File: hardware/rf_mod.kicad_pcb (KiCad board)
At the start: 4 copper layers, 100 x 100 mm, 63 parts, among them J1201 SMA, J1202 SMA, J201 SMA, J202 SMA, J401 SMA, J402 SMA, J501 SMA, J502 SMA, J901 USB-C, J902 SMA, Q1201 AO3401A, Q501 AO3401A, SW1201 ON, SW501 ON, U1201 GALI-84+, U501 GALI-84+, U901 MT3608, U902 3.3V, U903 74LVC1G17, X901 25 MHz

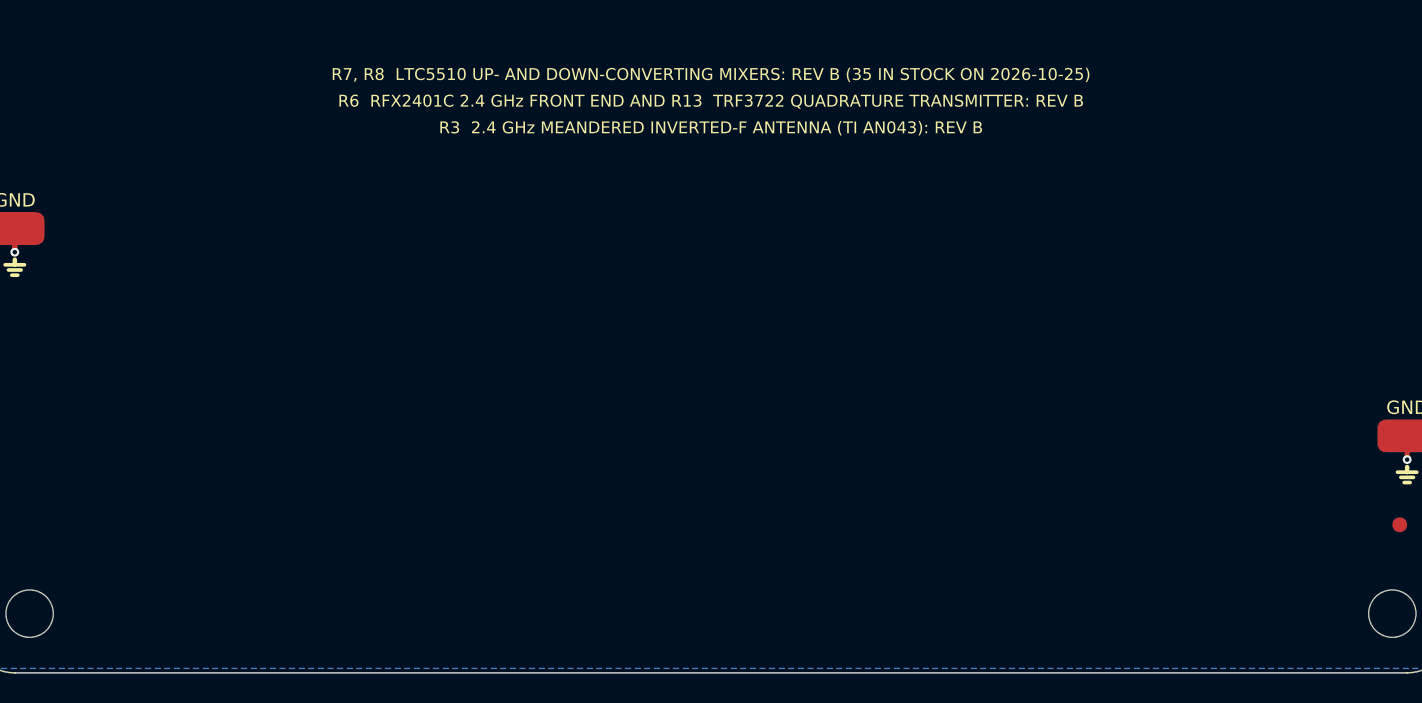
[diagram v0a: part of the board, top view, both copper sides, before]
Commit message: RF-MOD: the two MAX2871 synthesizer tiles (R10 host of the Pmod plug, R11) at DRC 0; a Fine net class at 0.127 mm with 0.45/0.25 vias for the QFN fan-out, V33 islands on L3, FRONT_WIRES; the fab package passes
Co-Authored-By: Claude Fable 5.1 <noreply@anthropic.com>
Claude-Session: https://claude.ai/code/session_01RKeoKvFFzjk3cEBLCXXHnB
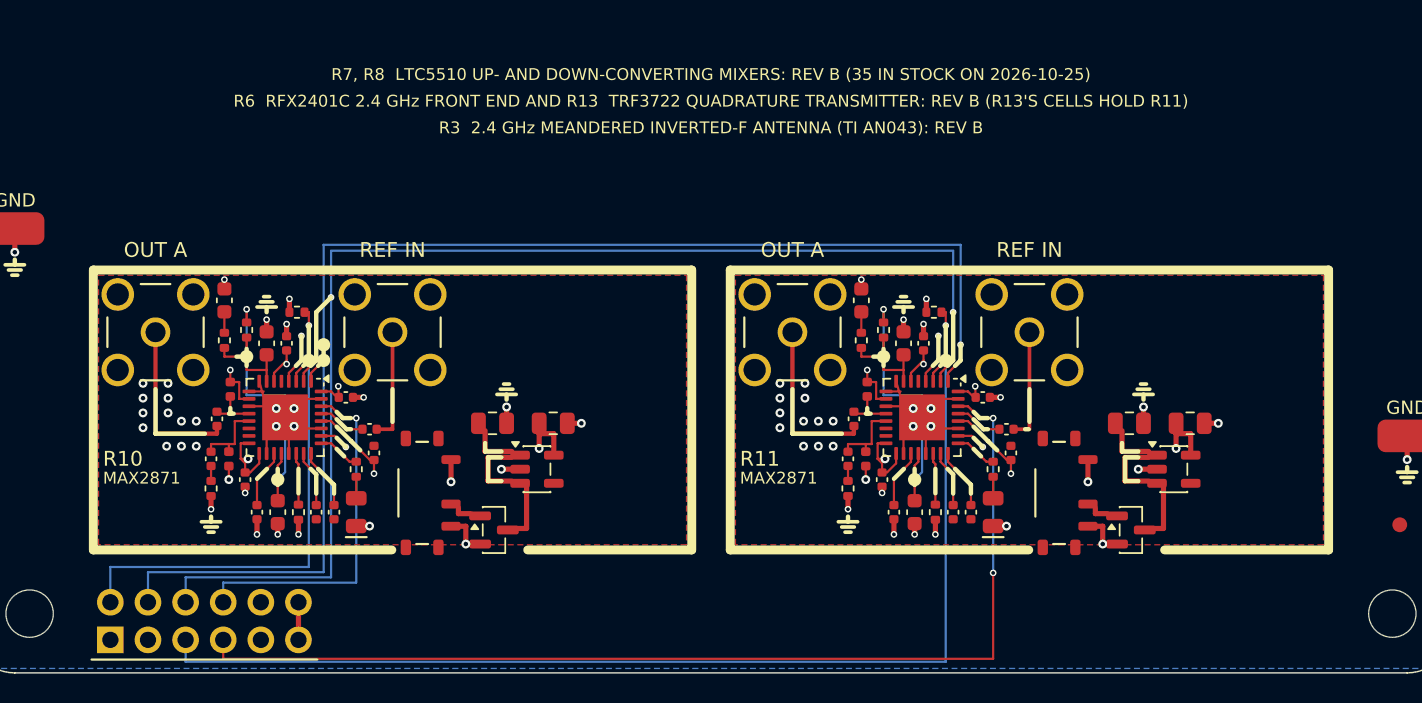
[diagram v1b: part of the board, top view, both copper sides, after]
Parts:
- added C1001: 1u, Capacitor_SMD:C_0805_2012Metric, F.Cu at (35.2, 83.2)
- added C1002: 1u, Capacitor_SMD:C_0805_2012Metric, F.Cu at (39.4, 83.2)
- added C1003: 470p, Capacitor_SMD:C_0603_1608Metric, F.Cu at (20.0, 77.8)
- added C1004: 6.8n, Capacitor_SMD:C_0603_1608Metric, F.Cu at (17.1, 74.8)
- added C1005: 100n, Capacitor_SMD:C_0402_1005Metric, F.Cu at (21.4, 77.8)
- added C1006: 100n, Capacitor_SMD:C_0402_1005Metric, F.Cu at (25.4, 81.4)
- added C1007: 100n, Capacitor_SMD:C_0402_1005Metric, F.Cu at (26.9, 83.5)
- added C1008: 100n, Capacitor_SMD:C_0402_1005Metric, F.Cu at (27.2, 85.2)
- added C1009: 100p, Capacitor_SMD:C_0402_1005Metric, F.Cu at (16.6, 82.8)
- added C1010: 100p, Capacitor_SMD:C_0402_1005Metric, F.Cu at (16.2, 85.5)
- added C1011: 100n, Capacitor_SMD:C_0402_1005Metric, F.Cu at (18.6, 87.0)
- added C1012: 1u, Capacitor_SMD:C_0402_1005Metric, F.Cu at (19.4, 89.2)
- added C1013: 100p, Capacitor_SMD:C_0603_1608Metric, F.Cu at (20.8, 89.2)
- added C1014: 1u, Capacitor_SMD:C_0402_1005Metric, F.Cu at (23.4, 89.2)
- added C1015: 1u, Capacitor_SMD:C_0402_1005Metric, F.Cu at (24.6, 89.2)
- added C1101: 1u, Capacitor_SMD:C_0805_2012Metric, F.Cu at (78.2, 83.2)
- added C1102: 1u, Capacitor_SMD:C_0805_2012Metric, F.Cu at (82.3, 83.2)
- added C1103: 470p, Capacitor_SMD:C_0603_1608Metric, F.Cu at (63.0, 77.8)
- added C1104: 6.8n, Capacitor_SMD:C_0603_1608Metric, F.Cu at (60.1, 74.8)
- added C1105: 100n, Capacitor_SMD:C_0402_1005Metric, F.Cu at (64.3, 77.8)
- added C1106: 100n, Capacitor_SMD:C_0402_1005Metric, F.Cu at (68.3, 81.4)
- added C1107: 100n, Capacitor_SMD:C_0402_1005Metric, F.Cu at (70.0, 83.5)
- added C1108: 100n, Capacitor_SMD:C_0402_1005Metric, F.Cu at (70.2, 85.2)
- added C1109: 100p, Capacitor_SMD:C_0402_1005Metric, F.Cu at (59.6, 82.8)
- added C1110: 100p, Capacitor_SMD:C_0402_1005Metric, F.Cu at (59.2, 85.5)
- added C1111: 100n, Capacitor_SMD:C_0402_1005Metric, F.Cu at (61.5, 87.0)
- added C1112: 1u, Capacitor_SMD:C_0402_1005Metric, F.Cu at (62.4, 89.2)
- added C1113: 100p, Capacitor_SMD:C_0603_1608Metric, F.Cu at (63.8, 89.2)
- added C1114: 1u, Capacitor_SMD:C_0402_1005Metric, F.Cu at (66.3, 89.2)
- added C1115: 1u, Capacitor_SMD:C_0402_1005Metric, F.Cu at (67.5, 89.2)
- added J1001: SMA, amod:SMA_BWSMA-KE-Z001_Vertical, F.Cu at (12.5, 77.0)
- added J1002: SMA, amod:SMA_BWSMA-KE-Z001_Vertical, F.Cu at (28.5, 77.0)
- added J1003: Pmod, amod:PinHeader_2x06_P2.54mm_Horizontal_PZ254R-12-12P, F.Cu at (15.8, 96.5)
- added J1101: SMA, amod:SMA_BWSMA-KE-Z001_Vertical, F.Cu at (55.5, 77.0)
- added J1102: SMA, amod:SMA_BWSMA-KE-Z001_Vertical, F.Cu at (71.5, 77.0)
- added L1001: 27n, Inductor_SMD:L_0402_1005Metric, F.Cu at (17.6, 80.8)
- added L1002: 27n, Inductor_SMD:L_0402_1005Metric, F.Cu at (17.4, 85.5)
- added L1101: 27n, Inductor_SMD:L_0402_1005Metric, F.Cu at (60.5, 80.8)
- added L1102: 27n, Inductor_SMD:L_0402_1005Metric, F.Cu at (60.5, 85.5)
- added LED1001: LOCK, amod:LED_0805_2012Metric_Kbar, F.Cu at (26.1, 89.2)
- added LED1101: LOCK, amod:LED_0805_2012Metric_Kbar, F.Cu at (69.0, 89.2)
- added Q1001: AO3401A, Package_TO_SOT_SMD:SOT-23, F.Cu at (35.4, 90.3)
- added Q1101: AO3401A, Package_TO_SOT_SMD:SOT-23, F.Cu at (78.3, 90.3)
- added R1001: 470, Resistor_SMD:R_0402_1005Metric, F.Cu at (18.6, 76.8)
- added R1002: 820, Resistor_SMD:R_0402_1005Metric, F.Cu at (17.1, 77.5)
- added R1003: 100k, Resistor_SMD:R_0402_1005Metric, F.Cu at (22.1, 75.7)
- added R1004: 1k, Resistor_SMD:R_0402_1005Metric, F.Cu at (26.1, 86.2)
- added R1005: 51R, Resistor_SMD:R_0402_1005Metric, F.Cu at (16.2, 87.5)
- added R1006: 5.1k, Resistor_SMD:R_0402_1005Metric, F.Cu at (22.1, 89.2)
- added R1101: 470, Resistor_SMD:R_0402_1005Metric, F.Cu at (61.6, 76.8)
- added R1102: 820, Resistor_SMD:R_0402_1005Metric, F.Cu at (60.1, 77.5)
- added R1103: 100k, Resistor_SMD:R_0402_1005Metric, F.Cu at (65.0, 75.7)
- added R1104: 1k, Resistor_SMD:R_0402_1005Metric, F.Cu at (69.0, 86.2)
- added R1105: 51R, Resistor_SMD:R_0402_1005Metric, F.Cu at (59.2, 87.5)
- added R1106: 5.1k, Resistor_SMD:R_0402_1005Metric, F.Cu at (65.2, 89.2)
- added SW1001: ON, amod:SW_SPDT_Shouhan_MSK12C02, F.Cu at (30.5, 87.8)
- added SW1101: ON, amod:SW_SPDT_Shouhan_MSK12C02, F.Cu at (73.5, 87.8)
- added U1001: 3.3V, Package_TO_SOT_SMD:SOT-23-5, F.Cu at (38.2, 86.2)
- added U1002: MAX2871, Package_DFN_QFN:QFN-32-1EP_5x5mm_P0.5mm_EP3.1x3.1mm, F.Cu at (21.2, 82.8)
- added U1101: 3.3V, Package_TO_SOT_SMD:SOT-23-5, F.Cu at (81.2, 86.2)
- added U1102: MAX2871, Package_DFN_QFN:QFN-32-1EP_5x5mm_P0.5mm_EP3.1x3.1mm, F.Cu at (64.2, 82.8)
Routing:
- net /PMOD6: track 0.00 -> 91.4 mm, vias 0 -> 2
- net /PMOD7: track 0.00 -> 91.1 mm, vias 0 -> 2
- net /PMOD3: track 0.00 -> 80.8 mm, vias 0 -> 1
- net /PMOD4: track 0.00 -> 72.2 mm, vias 0 -> 2
- net GND: track 55.4 -> 105.4 mm, vias 92 -> 154
- net /PMOD5: track 0.00 -> 37.4 mm, vias 0 -> 1
- net /R10_V33: track 0.00 -> 29.5 mm, vias 0 -> 9
- net /R11_V33: track 0.00 -> 29.5 mm, vias 0 -> 9
- net /PMOD8: track 0.00 -> 24.1 mm, vias 0 -> 1
- net /R11_TN: track 0.00 -> 18.5 mm, vias 0 -> 2
- net /R10_TN: track 0.00 -> 18.5 mm, vias 0 -> 2
- net /R11_OUTA: track 0.00 -> 11.5 mm
- net /R10_OUTA: track 0.00 -> 11.5 mm
- net /R11_VS: track 0.00 -> 11.4 mm
- net /R10_VS: track 0.00 -> 11.4 mm
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- added copper zone on In2.Cu, net /R10_V33
- added copper zone on In2.Cu, net /R11_V33
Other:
- board text added: "MAX2871"
- board text added: "OUT A"
- board text added: "R10"
- board text added: "R11"
- board text added: "R6 RFX2401C 2.4 GHz FRONT END AND R13 TRF3722 QUADRATURE TRANSMITTER: REV B (R13'S CELLS HOLD R11)"
- board text added: "REF IN"
- board text removed: "R6 RFX2401C 2.4 GHz FRONT END AND R13 TRF3722 QUADRATURE TRANSMITTER: REV B"

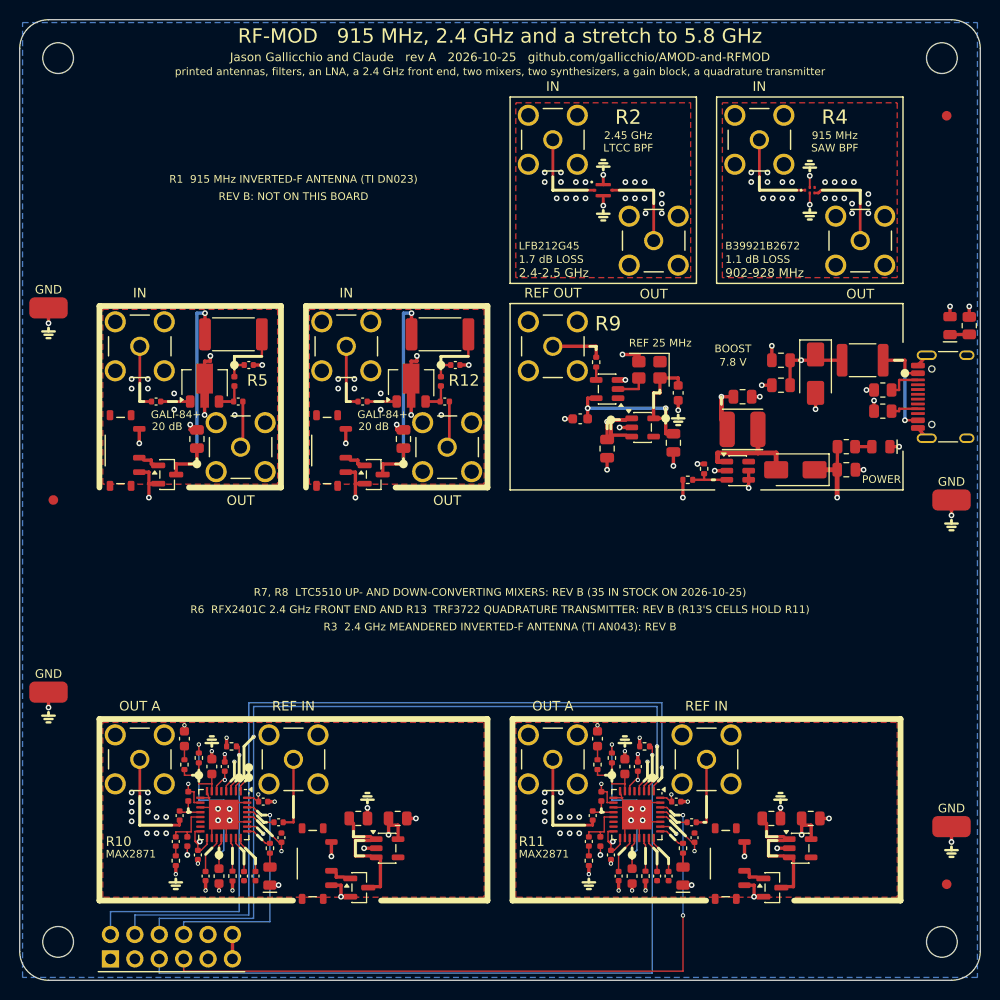
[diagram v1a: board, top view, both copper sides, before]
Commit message: RF-MOD filled: ADL5350 mixers R7/R8, a resistive splitter R1, ten tiles on sixteen cells at ERC/DRC 0 and the fab package passing; stand-in 3D bodies scaled 1/2.54 (VRML unit) on every board
Co-Authored-By: Claude Opus 5.5 <noreply@anthropic.com>
Claude-Session: https://claude.ai/code/session_01RKeoKvFFzjk3cEBLCXXHnB
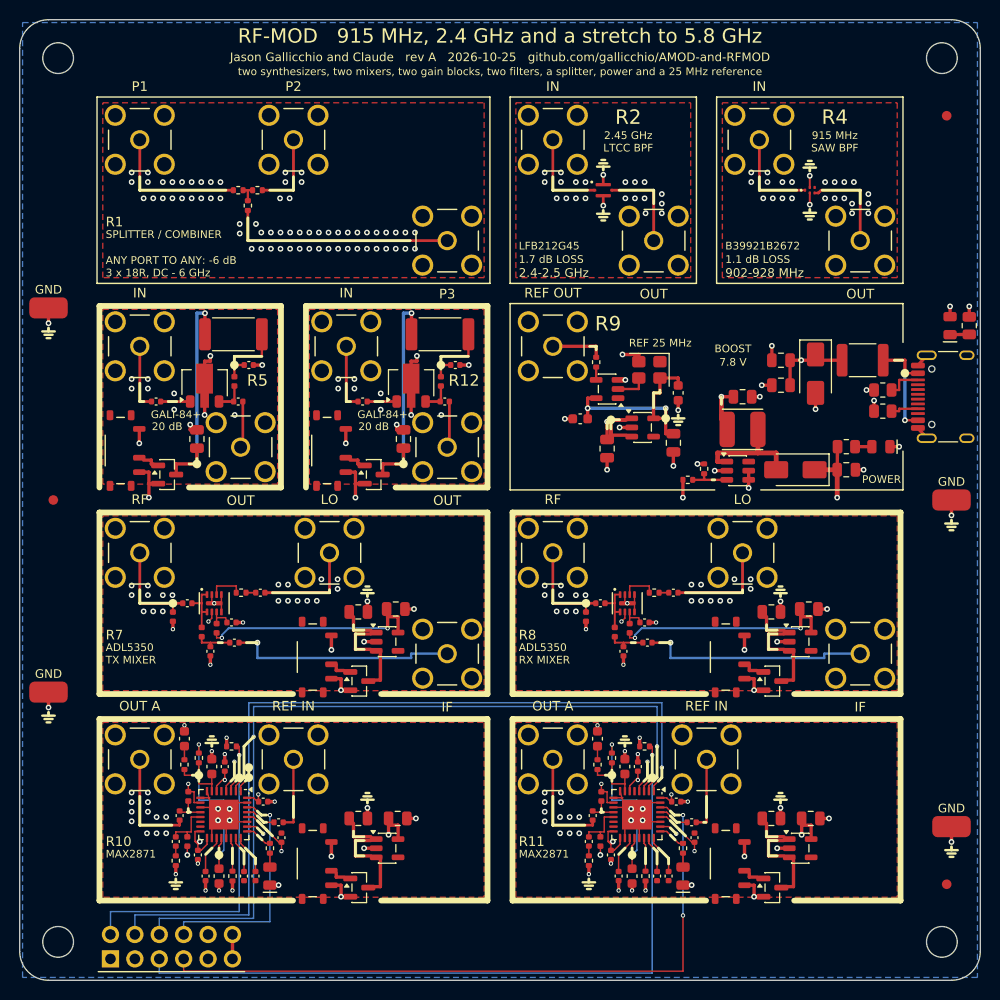
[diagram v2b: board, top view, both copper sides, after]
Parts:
- added C701: 1u, Capacitor_SMD:C_0805_2012Metric, F.Cu at (35.2, 61.6)
- added C702: 4.7u, Capacitor_SMD:C_0805_2012Metric, F.Cu at (39.1, 61.4)
- added C703: 15p, Capacitor_SMD:C_0402_1005Metric, F.Cu at (17.4, 60.8)
- added C704: 15p, Capacitor_SMD:C_0402_1005Metric, F.Cu at (19.9, 65.8)
- added C705: 100n, Capacitor_SMD:C_0402_1005Metric, F.Cu at (22.4, 64.8)
- added C706: 100p, Capacitor_SMD:C_0402_1005Metric, F.Cu at (25.1, 59.6)
- added C707: 100p, Capacitor_SMD:C_0402_1005Metric, F.Cu at (22.1, 62.8)
- added C801: 1u, Capacitor_SMD:C_0805_2012Metric, F.Cu at (78.2, 61.6)
- added C802: 4.7u, Capacitor_SMD:C_0805_2012Metric, F.Cu at (82.2, 61.4)
- added C803: 15p, Capacitor_SMD:C_0402_1005Metric, F.Cu at (60.5, 60.8)
- added C804: 15p, Capacitor_SMD:C_0402_1005Metric, F.Cu at (62.9, 65.8)
- added C805: 100n, Capacitor_SMD:C_0402_1005Metric, F.Cu at (65.3, 64.8)
- added C806: 100p, Capacitor_SMD:C_0402_1005Metric, F.Cu at (68.0, 59.6)
- added C807: 100p, Capacitor_SMD:C_0402_1005Metric, F.Cu at (65.0, 62.8)
- added J101: SMA, amod:SMA_BWSMA-KE-Z001_Vertical, F.Cu at (12.5, 12.5)
- added J102: SMA, amod:SMA_BWSMA-KE-Z001_Vertical, F.Cu at (28.5, 12.5)
- added J103: SMA, amod:SMA_BWSMA-KE-Z001_Vertical, F.Cu at (44.5, 23.0)
- added J701: SMA, amod:SMA_BWSMA-KE-Z001_Vertical, F.Cu at (12.5, 55.5)
- added J702: SMA, amod:SMA_BWSMA-KE-Z001_Vertical, F.Cu at (32.2, 55.5)
- added J703: SMA, amod:SMA_BWSMA-KE-Z001_Vertical, F.Cu at (44.5, 66.0)
- added J801: SMA, amod:SMA_BWSMA-KE-Z001_Vertical, F.Cu at (55.5, 55.5)
- added J802: SMA, amod:SMA_BWSMA-KE-Z001_Vertical, F.Cu at (75.2, 55.5)
- added J803: SMA, amod:SMA_BWSMA-KE-Z001_Vertical, F.Cu at (87.5, 66.0)
- added L701: 47n, Inductor_SMD:L_0402_1005Metric, F.Cu at (15.9, 62.1)
- added L702: 47n, Inductor_SMD:L_0402_1005Metric, F.Cu at (18.9, 63.8)
- added L703: 10n, Inductor_SMD:L_0402_1005Metric, F.Cu at (20.5, 63.4)
- added L801: 47n, Inductor_SMD:L_0402_1005Metric, F.Cu at (59.0, 62.1)
- added L802: 47n, Inductor_SMD:L_0402_1005Metric, F.Cu at (62.0, 63.8)
- added L803: 10n, Inductor_SMD:L_0402_1005Metric, F.Cu at (63.5, 63.4)
- added Q701: AO3401A, Package_TO_SOT_SMD:SOT-23, F.Cu at (35.4, 68.8)
- added Q801: AO3401A, Package_TO_SOT_SMD:SOT-23, F.Cu at (78.3, 68.8)
- added R101: 18R, Resistor_SMD:R_0402_1005Metric, F.Cu at (22.8, 17.8)
- added R102: 18R, Resistor_SMD:R_0402_1005Metric, F.Cu at (24.8, 17.8)
- added R103: 18R, Resistor_SMD:R_0402_1005Metric, F.Cu at (23.8, 19.4)
- added R701: 0R, Resistor_SMD:R_0402_1005Metric, F.Cu at (23.1, 59.6)
- added R801: 0R, Resistor_SMD:R_0402_1005Metric, F.Cu at (66.0, 59.6)
- added SW701: ON, amod:SW_SPDT_Shouhan_MSK12C02, F.Cu at (30.5, 66.3)
- added SW801: ON, amod:SW_SPDT_Shouhan_MSK12C02, F.Cu at (73.5, 66.3)
- added U701: 3.3V, Package_TO_SOT_SMD:SOT-23-5, F.Cu at (38.2, 64.8)
- added U702: ADL5350, amod:LFCSP-8_2x3mm_P0.5mm_ADL5350, F.Cu at (20.2, 60.8)
- added U801: 3.3V, Package_TO_SOT_SMD:SOT-23-5, F.Cu at (81.2, 64.8)
- added U802: ADL5350, amod:LFCSP-8_2x3mm_P0.5mm_ADL5350, F.Cu at (63.2, 60.8)
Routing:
- net /R1_P3: track 0.00 -> 23.9 mm
- net /R8_IF: track 0.00 -> 23.7 mm, vias 0 -> 1
- net /R7_IF: track 0.00 -> 23.7 mm, vias 0 -> 1
- net /R7_V33: track 0.00 -> 23.6 mm, vias 0 -> 2
- net /R8_V33: track 0.00 -> 23.6 mm, vias 0 -> 2
- net GND: track 105.4 -> 127.6 mm, vias 154 -> 274
- net /R1_P1: track 0.00 -> 15.0 mm
- net /R8_VS: track 0.00 -> 11.4 mm
- net /R7_VS: track 0.00 -> 11.4 mm
- net /R8_LOJ: track 0.00 -> 10.9 mm
- net /R7_LOJ: track 0.00 -> 10.9 mm
- net /R8_RFN: track 0.00 -> 10.6 mm
- net /R7_RFN: track 0.00 -> 10.6 mm
- net /R1_P2: track 0.00 -> 8.49 mm
- net +5V: track 31.9 -> 38.2 mm, vias 7 -> 9
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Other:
- board text added: "3 x 18R, DC - 6 GHz"
- board text added: "ADL5350"
- board text added: "ANY PORT TO ANY: -6 dB"
- board text added: "IF"
- board text added: "LO"
- board text added: "P1"
- board text added: "P2"
- board text added: "P3"
- board text added: "R1"
- board text added: "R7"
- board text added: "R8"
- board text added: "RF"
- board text added: "RX MIXER"
- board text added: "SPLITTER / COMBINER"
- board text added: "TX MIXER"
- board text added: "jack, OUT its bottom-right; the powered tiles have a slide"
- board text added: "switch (up: on). Power: USB-C on R9. The handbook has"
- board text added: "the rest."
- board text added: "two synthesizers, two mixers, two gain blocks, two filters, a splitter, power and a 25 MHz reference"
- board text removed: "R1 915 MHz INVERTED-F ANTENNA (TI DN023)"
- board text removed: "R3 2.4 GHz MEANDERED INVERTED-F ANTENNA (TI AN043): REV B"
- board text removed: "R6 RFX2401C 2.4 GHz FRONT END AND R13 TRF3722 QUADRATURE TRANSMITTER: REV B (R13'S CELLS HOLD R11)"
- board text removed: "R7, R8 LTC5510 UP- AND DOWN-CONVERTING MIXERS: REV B (35 IN STOCK ON 2026-10-25)"
- board text removed: "REV B: NOT ON THIS BOARD"
- board text removed: "The handbook has the rest."
- board text removed: "have a slide switch (up: on). Power: USB-C on R9."
- board text removed: "jack, OUT its bottom-right; the gain blocks and synthesizers"
- board text removed: "printed antennas, filters, an LNA, a 2.4 GHz front end, two mixers, two synthesizers, a gain block, a quadrature transmitter"

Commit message: Pmod plugs: fix the mirrored pinout on AMOD-A and RF-MOD (JLCPCB's numbering of the PZ254R runs opposite to KiCad's): plug two columns left, nets renamed to the standard IO numbers, a fab check of every plug pad; mounting holes replaced by four marked rubber feet on both boards
Co-Authored-By: Claude Opus 5.5 <noreply@anthropic.com>
Claude-Session: https://claude.ai/code/session_01RKeoKvFFzjk3cEBLCXXHnB
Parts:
- removed MH1, MH2, MH3, MH4: MountingHole, MountingHole:MountingHole_3.2mm_M3
- moved J1003 5.08 mm to (10.7, 96.5)
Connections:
- J1003 pad 1: unconnected-(J1003-Pin_1-Pad1) -> /PMOD_VCC
- J1003 pad 10: GND -> /PMOD2
- J1003 pad 11: /PMOD_VCC -> /PMOD5
- J1003 pad 12: /PMOD_VCC -> /PMOD1
- J1003 pad 2: /PMOD5 -> /PMOD_VCC
- J1003 pad 3: unconnected-(J1003-Pin_3-Pad3) -> GND
- J1003 pad 4: /PMOD6 -> GND
- J1003 pad 5: /PMOD3 -> unconnected-(J1003-Pin_5-Pad5)
- J1003 pad 6: /PMOD7 -> /PMOD4
- J1003 pad 7: /PMOD4 -> unconnected-(J1003-Pin_7-Pad7)
- J1003 pad 8: /PMOD8 -> /PMOD3
- J1003 pad 9: GND -> /PMOD6
- R1003 pad 2: /PMOD5 -> /PMOD4
- R1103 pad 2: /PMOD3 -> /PMOD6
- U1002 pad 1: /PMOD6 -> /PMOD3
- U1002 pad 2: /PMOD7 -> /PMOD2
- U1002 pad 3: /PMOD5 -> /PMOD4
- U1002 pad 30: /PMOD8 -> /PMOD1
- U1102 pad 1: /PMOD6 -> /PMOD3
- U1102 pad 2: /PMOD7 -> /PMOD2
- U1102 pad 3: /PMOD3 -> /PMOD6
- U1102 pad 30: /PMOD4 -> /PMOD5
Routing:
- net /PMOD7: track 91.1 -> 0.00 mm, vias 2 -> 0
- net /PMOD2: track 0.00 -> 91.1 mm, vias 0 -> 2
- net /PMOD5: track 37.4 -> 72.2 mm, vias 1 -> 2
- net /PMOD4: track 72.2 -> 37.4 mm, vias 2 -> 1
- net /PMOD8: track 24.1 -> 0.00 mm, vias 1 -> 0
- net /PMOD1: track 0.00 -> 24.1 mm, vias 0 -> 1
- net /PMOD6: track 91.4 -> 80.8 mm, vias 2 -> 1
- net /PMOD3: track 80.8 -> 91.4 mm, vias 1 -> 2
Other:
- board text added: "FOOT"
